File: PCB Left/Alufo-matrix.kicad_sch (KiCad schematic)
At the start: 59 parts, among them K11 PG1350, K12 PG1350, K13 PG1350, K14 PG1350, K15 PG1350, K16 PG1350, K21 PG1350, K22 PG1350, K23 PG1350, K24 PG1350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

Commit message: Add LCSC part numbers to left side
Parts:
- D11, D12, D13, D14, D15, D16, D21, D22, D23, D24, D25, D26, D31, D32, D33, D34, D35, D36: LCSC (none) -> C917030
- K11, K12, K13, K14, K15, K16, K21, K22, K23, K24, K25, K26, K31, K32, K33, K34, K35, K36: LCSC (none) -> C5333465; now not fitted
- PK11, PK12, PK13, PK14, PK15, PK16, PK21, PK22, PK23, PK24, PK25, PK26, PK31, PK32, PK33, PK34, PK35, PK36: now not fitted
- R12, R13, R14, R15, R16: LCSC (none) -> C2960848

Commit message: Update project library name in schematic
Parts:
- D11, D12, D13, D14, D15, D16, D21, D22, D23, D24, D25, D26, D31, D32, D33, D34, D35, D36: footprint Project Library:D_SOD-123_Mod -> Project_Library:D_SOD-123_Mod
- K11, K12, K13, K14, K15, K16, K21, K22, K23, K24, K25, K26, K31, K32, K33, K34, K35: footprint Project Library:SW_choc_v1_HS_CPG135001S30_1layer_1u -> Project_Library:SW_choc_v1_HS_CPG135001S30_1layer_1u
- K36: footprint Project Library:SW_choc_v1_HS_CPG135001S30_1layer_1.5u -> Project_Library:SW_choc_v1_HS_CPG135001S30_1layer_1.5u
- PK11, PK12, PK13, PK14, PK15, PK16, PK21, PK22, PK23, PK24, PK25, PK26, PK31, PK32, PK33, PK34, PK35: footprint Project Library:SW_choc_v1_Plate_CPG135001S30_1u -> Project_Library:SW_choc_v1_Plate_CPG135001S30_1u
- PK36: footprint Project Library:SW_choc_v1_Plate_CPG135001S30_1.5u -> Project_Library:SW_choc_v1_Plate_CPG135001S30_1.5u

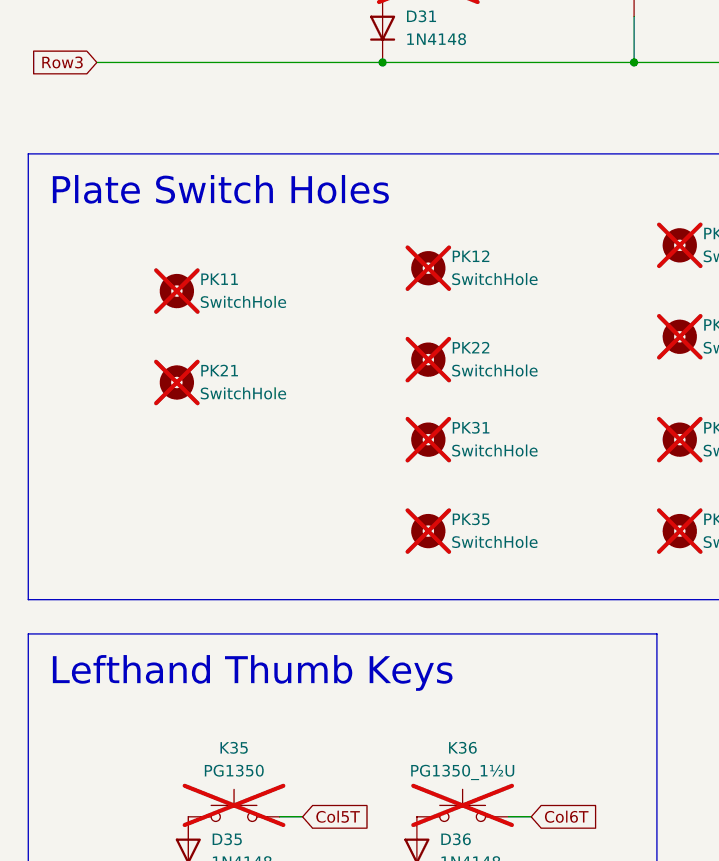
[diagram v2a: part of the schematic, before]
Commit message: Update to KiCad v9
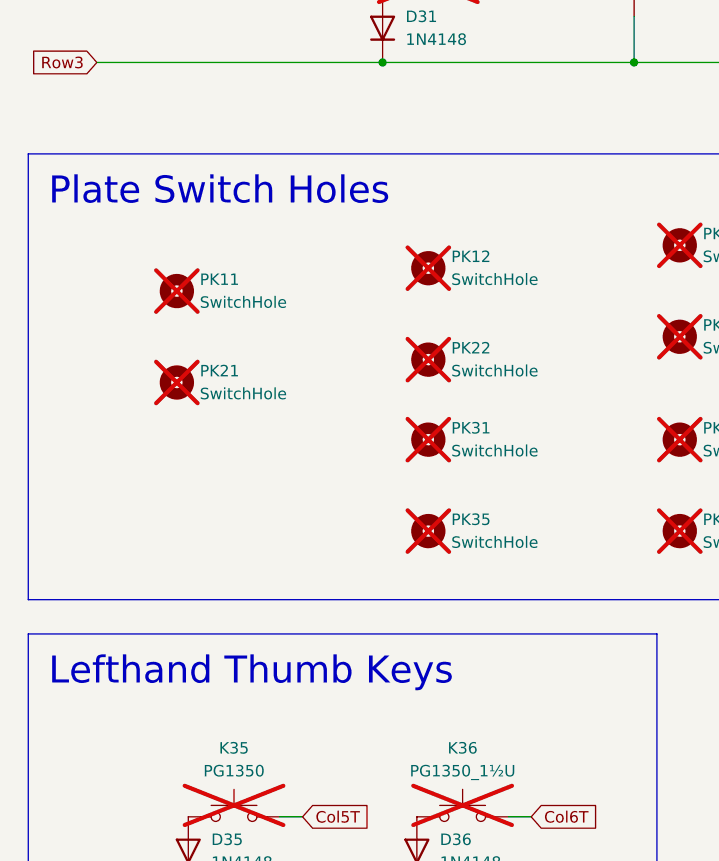
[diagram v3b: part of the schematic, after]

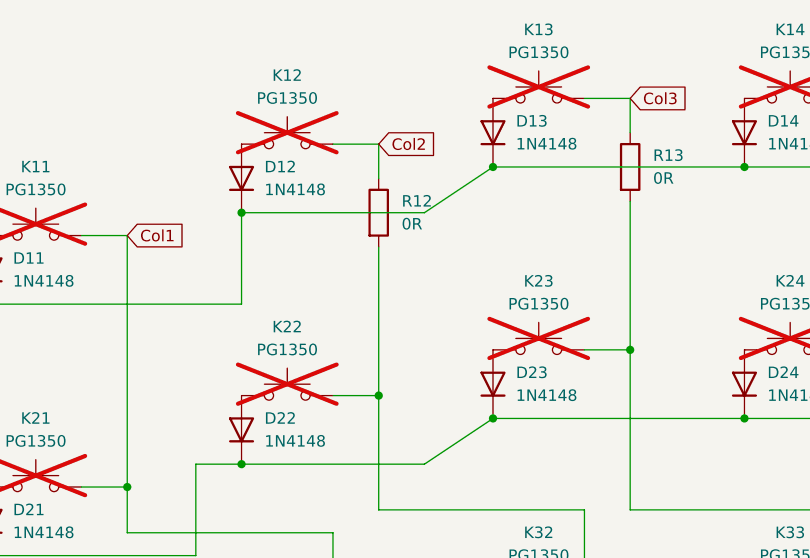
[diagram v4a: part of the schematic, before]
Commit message: Remove lefthand R12
Can route Col1, Col2 and Row2 around each other without needing jumper on Col2.
Col1 and Col2 pins on MCU swapped.
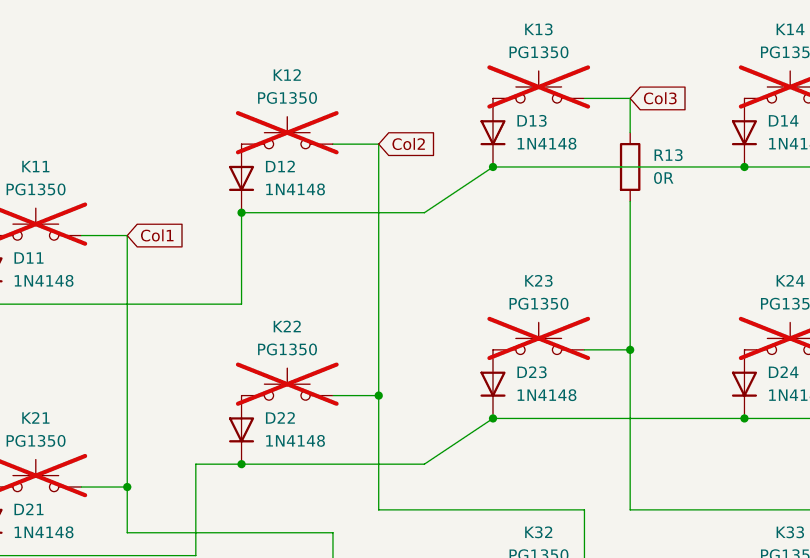
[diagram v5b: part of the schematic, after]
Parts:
- removed R12: 0R, Resistor_SMD:R_2010_5025Metric, symbol Device:R
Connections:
- net Col2: now also K22.1, K32.1
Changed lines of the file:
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@@
-	(wire
-		(pts
-			(xy 115.57 44.45) (xy 115.57 60.96)
-		)
-		(stroke
-			(width 0)
-			(type default)
-		)
-	)
 	(wire
 		(pts
@@
 	(wire
 		(pts
-			(xy 115.57 33.02) (xy 115.57 36.83)
+			(xy 115.57 33.02) (xy 115.57 60.96)
 		)
 		(stroke
@@
 					(unit 1)
 				)
-			)
-		)
-	)
-	(symbol
-		(lib_id "Device:R")
-		(at 115.57 40.64 0)
-		(unit 1)
-		(exclude_from_sim no)
-		(in_bom yes)
-		(on_board yes)
-		(dnp no)
-		(property "Reference" "R12"
-			(at 118.11 39.3699 0)
-			(effects
-				(font
-					(size 1.27 1.27)
-				)
-				(justify left)
-			)
-		)
-		(property "Value" "0R"
-			(at 118.11 41.9099 0)
-			(effects
-				(font
-					(size 1.27 1.27)
-				)
-				(justify left)
-			)
-		)
-		(property "Footprint" "Resistor_SMD:R_2010_5025Metric"
-			(at 113.792 40.64 90)
-			(effects
-				(font
-					(size 1.27 1.27)
-				)
-				(hide yes)
-			)
-		)
-		(property "Datasheet" "~"
-			(at 115.57 40.64 0)
-			(effects
-				(font
-					(size 1.27 1.27)
-				)
-				(hide yes)
-			)
-		)
-		(property "Description" "Resistor"
-			(at 115.57 40.64 0)
-			(effects
-				(font
-					(size 1.27 1.27)
-				)
-				(hide yes)
-			)
-		)
-		(property "LCSC" "C2960848"
-			(at 115.57 40.64 0)
-			(effects
-				(font
-					(size 1.27 1.27)
-				)
-				(hide yes)
-			)
-		)
-		(pin "1"
-		)
-		(pin "2"
-		)
-		(instances
-			(project "Alufo"
-				(path "/52f043ac-ccff-4c85-bc10-2db9d3c9e3f3/ba0213d9-9934-4194-9bec-bf394cd27126"
-					(reference "R12")
-					(unit 1)
-				)
